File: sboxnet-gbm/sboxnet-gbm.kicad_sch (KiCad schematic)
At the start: 55 parts, among them J1 Screw_Terminal_01x04, J2 Screw_Terminal_01x04, J3 Screw_Terminal_01x04, J4 sboxnet-stecker_02x17, J5 Screw_Terminal_01x04, J6 Conn_02x08_Top_Bottom, U1 LTV-844, U2 LTV-844, U3 LTV-844, U4 SN65HVD230

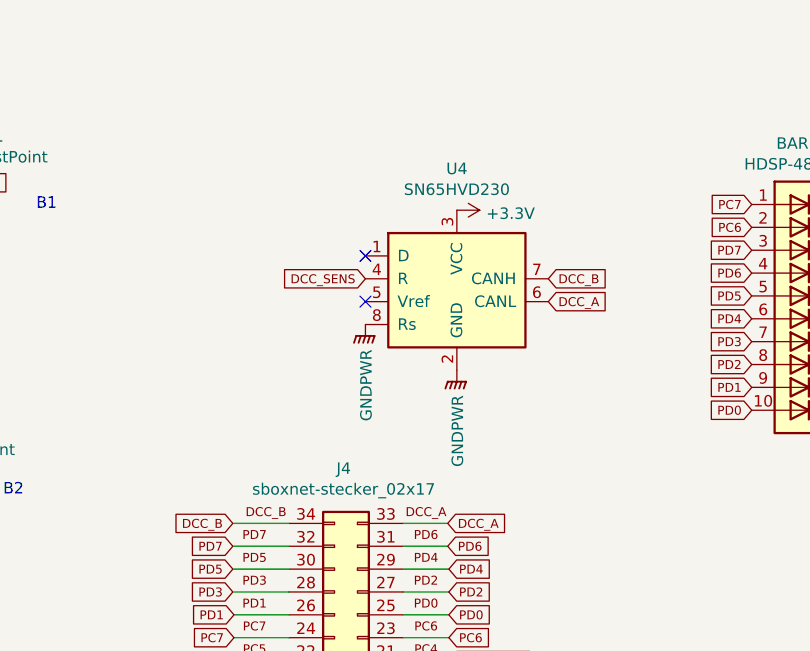
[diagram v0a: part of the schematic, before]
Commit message: kicad 5 -> 6
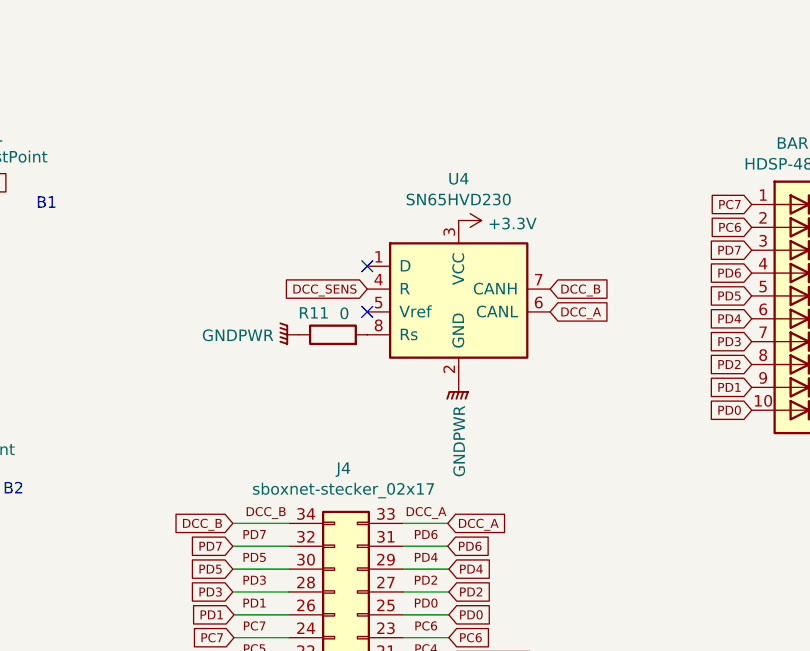
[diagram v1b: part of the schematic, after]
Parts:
- added R11: 0, Resistor_SMD:R_1206_3216Metric_Pad1.30x1.75mm_HandSolder, symbol Device:R
- U1, U2, U3: footprint Package_DIP:DIP-16_W7.62mm -> Package_SO:SOIC-16_4.55x10.3mm_P1.27mm
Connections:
- net GNDPWR: now also R11.1; no longer U4.8 (Rs)
- new net: R11.2, U4.8 (Rs)
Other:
- moved on the sheet: U4

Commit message: cleanup
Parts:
- removed JP1, JP2, JP3: SolderJumper_3_Open, Jumper:SolderJumper-3_P1.3mm_Open_RoundedPad1.0x1.5mm, symbol Jumper:SolderJumper_3_Open
- added JP1, JP2, JP3: SolderJumper_2_Open, Jumper:SolderJumper-2_P1.3mm_Open_TrianglePad1.0x1.5mm, symbol Jumper:SolderJumper_2_Open
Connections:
- net GNDPWR: now also JP1.2 (B), JP2.2 (B), JP3.2 (B)
- net PB0: now also JP3.1 (A)
- net PB1: now also JP2.1 (A)
- net PB2: now also JP1.1 (A)
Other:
- note added: "1"
- note added: "2"
- note added: "3"
- note added: "4"
- note added: "5"
- note added: "6"
- note added: "7"
- note added: "8"
- note added: "9"
- note added: "Pin 1 GND Pin 2 KEY_SEL Pin 3 KEY_ACT Pin 4 KEY_UP Pin 5 KEY_DOWN Pin 9 PD0 Pin 10 PD1 Pin 11 PD2 Pin 12 PD3 Pin 13 PD4 Pin 14 PD5 Pin 15 PD6 Pin 16 PD7"
- note removed: "Pin 1 GND Pin 2 KEY_SEL Pin 3 KEY_ACT Pin 4 KEY_UP Pin 5 KEY_DOWN Pin 7 PC6 Pin 8 PC7 Pin 9 PD7 Pin 10 PD6 Pin 11 PD5 Pin 12 PD4 Pin 13 PD3 Pin 14 PD2 Pin 15 PD1 Pin 16 PD0"
